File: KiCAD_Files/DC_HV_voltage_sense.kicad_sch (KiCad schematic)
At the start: 17 parts, among them U401 AMC1311BDWVR, U402 MCP6486UT-E/LT

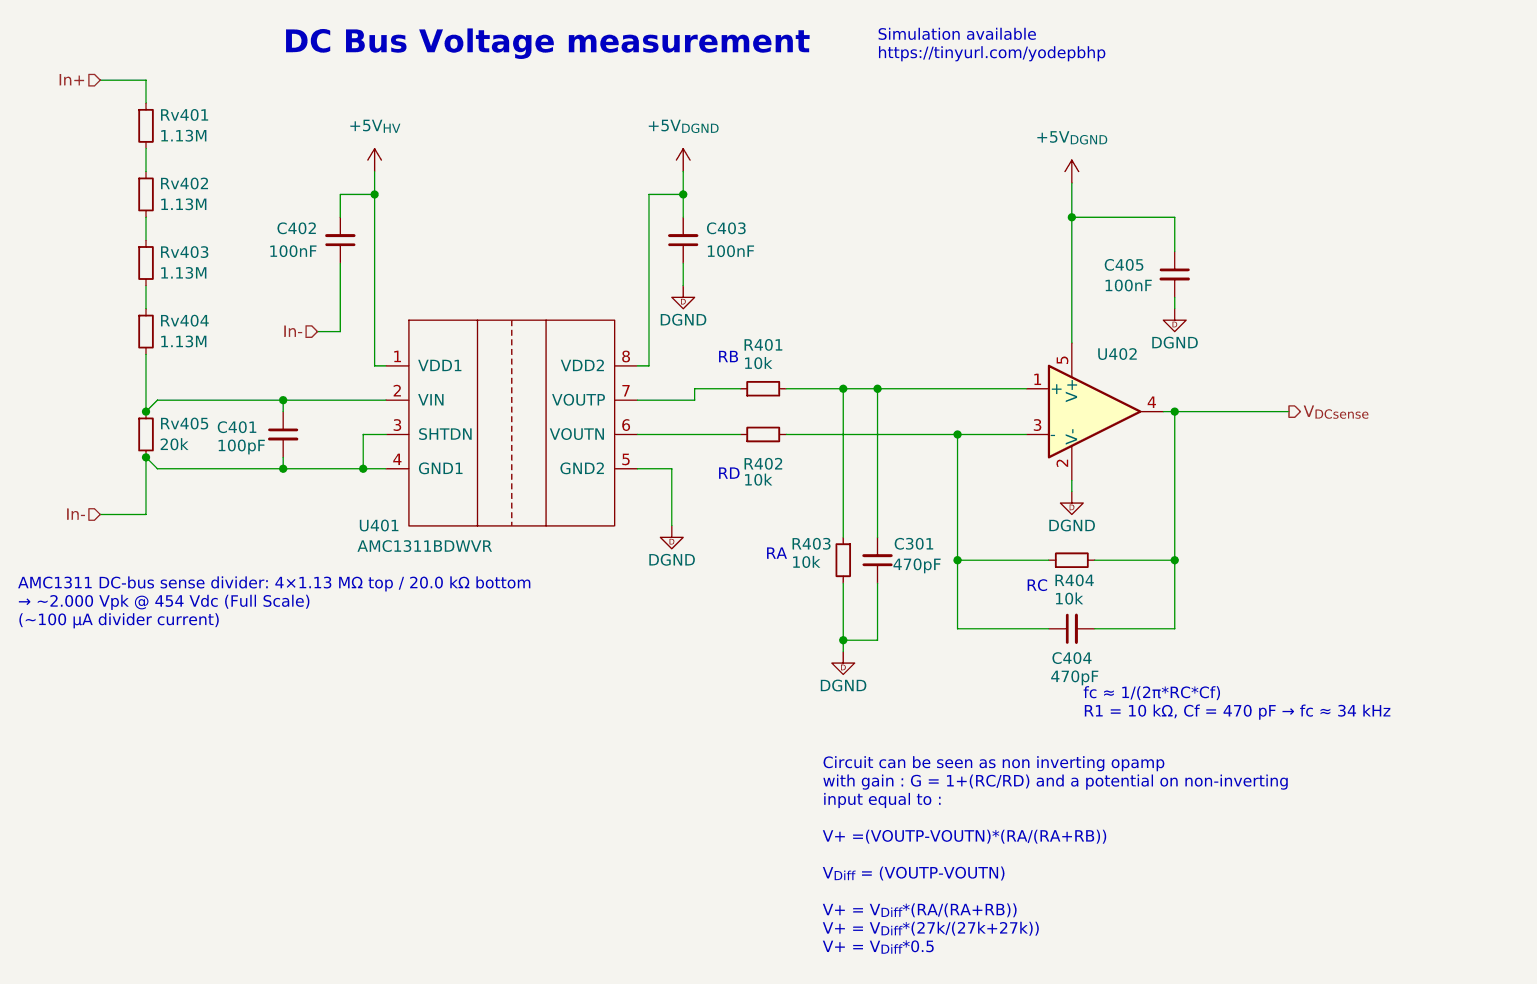
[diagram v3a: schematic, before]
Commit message: Added TL431 for AC measurement 5V regulation. Added more film capacitance. Increased size of 100V ceramic caps to 1210.
Signed-off-by: Jean Alinei <jean.alinei@owntech.org>
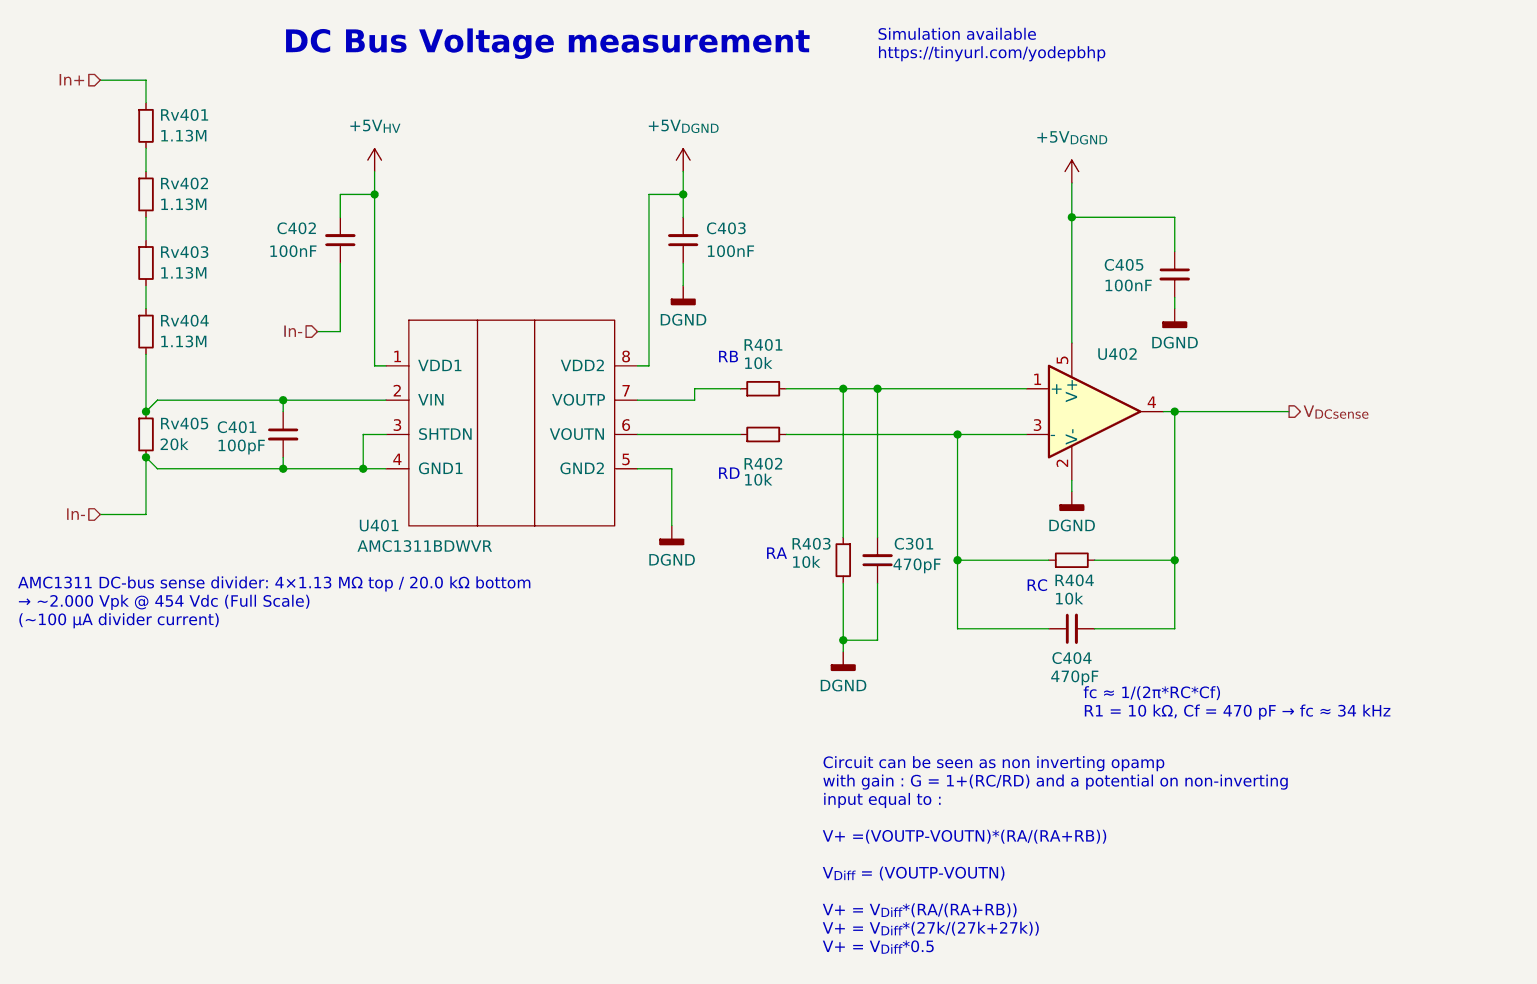
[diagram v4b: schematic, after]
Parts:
- U401: symbol Symbols:AMC1311DBW -> Symbols:AMC1311
- U402: footprint Package_TO_SOT_SMD:SOT-353_SC-70-5_Handsoldering -> Package_TO_SOT_SMD:SOT-353_SC-70-5; symbol Symbols:MCP6486UT-E/LT -> Symbols:MCP6486UT-E/LT
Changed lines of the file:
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@@
 			)
 		)
-		(property "Datasheet" "${KIPRJMOD}\\datasheet\\PYu_RT_1_to_0_01_RoHS_L_12-3003070.pdf"
+		(property "Datasheet" "~"
 			(at 135.89 105.41 0)
 			(effects
@@
 			)
 		)
-		(property "Description" ""
+		(property "Description" "Resistor, small symbol"
 			(at 135.89 105.41 0)
 			(effects
@@
 			)
 		)
-		(property "Description" ""
+		(property "Description" "Resistor, small symbol"
 			(at 33.02 72.39 0)
 			(effects
@@
 	)
 	(symbol
-		(lib_name "R_Small_14")
 		(lib_id "Device:R_Small")
 		(at 101.6 86.36 90)
@@
 			)
 		)
-		(property "Datasheet" "${KIPRJMOD}\\datasheet\\PYu_RT_1_to_0_01_RoHS_L_12-3003070.pdf"
+		(property "Datasheet" "~"
 			(at 101.6 86.36 0)
 			(effects
@@
 			)
 		)
-		(property "Description" ""
+		(property "Description" "Resistor, small symbol"
 			(at 101.6 86.36 0)
 			(effects
@@
 	)
 	(symbol
-		(lib_id "Symbols:DGND")
+		(lib_id "power:GNDD")
 		(at 92.71 74.93 0)
 		(unit 1)
@@
 			)
 		)
-		(property "Description" ""
+		(property "Description" "Power symbol creates a global label with name \"GNDD\" , digital ground"
 			(at 92.71 74.93 0)
 			(effects
@@
 	)
 	(symbol
-		(lib_id "Symbols:+12V_PGND")
+		(lib_id "power:+12V")
 		(at 92.71 62.23 0)
 		(unit 1)
 		(exclude_from_sim no)
-		(in_bom no)
-		(on_board no)
+		(in_bom yes)
+		(on_board yes)
 		(dnp no)
 		(fields_autoplaced yes)
@@
 		)
 		(property "Footprint" ""
-			(at 95.885 59.69 0)
+			(at 92.71 62.23 0)
 			(effects
 				(font
@@
 		)
 		(property "Datasheet" ""
-			(at 95.885 59.69 0)
-			(effects
-				(font
-					(size 1.27 1.27)
-				)
-				(hide yes)
-			)
-		)
-		(property "Description" ""
+			(at 92.71 62.23 0)
+			(effects
+				(font
+					(size 1.27 1.27)
+				)
+				(hide yes)
+			)
+		)
+		(property "Description" "Power symbol creates a global label with name \"+12V\""
 			(at 92.71 62.23 0)
 			(effects
@@
 			)
 		)
-		(property "Datasheet" "${KIPRJMOD}\\datasheet\\PYu_RT_1_to_0_01_RoHS_L_12-3003070.pdf"
+		(property "Datasheet" "~"
 			(at 110.49 105.41 0)
 			(effects
@@
 			)
 		)
-		(property "Description" ""
+		(property "Description" "Resistor, small symbol"
 			(at 110.49 105.41 0)
 			(effects
@@
 	)
 	(symbol
-		(lib_name "R_Small_14")
 		(lib_id "Device:R_Small")
 		(at 101.6 91.44 90)
@@
 			)
 		)
-		(property "Datasheet" "${KIPRJMOD}\\datasheet\\PYu_RT_1_to_0_01_RoHS_L_12-3003070.pdf"
+		(property "Datasheet" "~"
 			(at 101.6 91.44 0)
 			(effects
@@
 			)
 		)
-		(property "Description" ""
+		(property "Description" "Resistor, small symbol"
 			(at 101.6 91.44 0)
 			(effects
@@
 	)
 	(symbol
-		(lib_id "Symbols:DGND")
+		(lib_id "power:GNDD")
 		(at 91.44 101.6 0)
 		(unit 1)
@@
 			)
 		)
-		(property "Description" ""
+		(property "Description" "Power symbol creates a global label with name \"GNDD\" , digital ground"
 			(at 91.44 101.6 0)
 			(effects
@@
 			)
 		)
-		(property "Description" ""
+		(property "Description" "Resistor, small symbol"
 			(at 33.02 80.01 0)
 			(effects
@@
 	)
 	(symbol
-		(lib_id "Symbols:DGND")
+		(lib_id "power:GNDD")
 		(at 135.89 97.79 0)
 		(unit 1)
@@
 			)
 		)
-		(property "Description" ""
+		(property "Description" "Power symbol creates a global label with name \"GNDD\" , digital ground"
 			(at 135.89 97.79 0)
 			(effects
@@
 	)
 	(symbol
-		(lib_id "Symbols:DGND")
+		(lib_id "power:GNDD")
 		(at 147.32 77.47 0)
 		(unit 1)
@@
 			)
 		)
-		(property "Description" ""
+		(property "Description" "Power symbol creates a global label with name \"GNDD\" , digital ground"
 			(at 147.32 77.47 0)
 			(effects
@@
 	)
 	(symbol
-		(lib_name "AMC1311DBW_1")
-		(lib_id "Symbols:AMC1311DBW")
+		(lib_id "Symbols:AMC1311")
 		(at 73.66 91.44 0)
 		(unit 1)
@@
 		)
 		(property "Footprint" "Package_SO:SOIC-8_7.5x5.85mm_P1.27mm"
-			(at 76.2 68.58 0)
-			(effects
-				(font
-					(size 1.27 1.27)
-				)
-				(hide yes)
-			)
-		)
-		(property "Datasheet" "./datasheets/amc1311.pdf"
-			(at 102.87 71.12 0)
-			(effects
-				(font
-					(size 1.27 1.27)
-				)
-				(hide yes)
-			)
-		)
-		(property "Description" ""
+			(at 73.66 97.79 0)
+			(effects
+				(font
+					(size 1.27 1.27)
+				)
+				(hide yes)
+			)
+		)
+		(property "Datasheet" "https://www.ti.com/lit/ds/symlink/amc1311.pdf?ts=1597049043074&ref_url=https%253A%252F%252Fwww.google.com%252F"
+			(at 73.66 97.79 0)
+			(effects
+				(font
+					(size 1.27 1.27)
+				)
+				(hide yes)
+			)
+		)
+		(property "Description" "High-Impedance,2-V Input, Fixed gain:1 - Reinforced Isolated Amplifiers"
 			(at 73.66 91.44 0)
 			(effects
@@
 			)
 		)
-		(property "Description" ""
+		(property "Description" "Resistor, small symbol"
 			(at 33.02 91.44 0)
 			(effects
@@
 	)
 	(symbol
-		(lib_id "Symbols:+12V_PGND")
+		(lib_id "power:+12V")
 		(at 58.42 62.23 0)
 		(unit 1)
 		(exclude_from_sim no)
-		(in_bom no)
-		(on_board no)
+		(in_bom yes)
+		(on_board yes)
 		(dnp no)
 		(fields_autoplaced yes)
@@
 		)
 		(property "Footprint" ""
-			(at 61.595 59.69 0)
+			(at 58.42 62.23 0)
 			(effects
 				(font
@@
 		)
 		(property "Datasheet" ""
-			(at 61.595 59.69 0)
-			(effects
-				(font
-					(size 1.27 1.27)
-				)
-				(hide yes)
-			)
-		)
-		(property "Description" ""
+			(at 58.42 62.23 0)
+			(effects
+				(font
+					(size 1.27 1.27)
+				)
+				(hide yes)
+			)
+		)
+		(property "Description" "Power symbol creates a global label with name \"+12V\""
 			(at 58.42 62.23 0)
 			(effects
@@
 			)
 		)
-		(property "Description" ""
+		(property "Description" "Resistor, small symbol"
 			(at 33.02 64.77 0)
 			(effects
@@
 	)
 	(symbol
-		(lib_id "Symbols:+12V_PGND")
+		(lib_id "power:+12V")
 		(at 135.89 63.5 0)
 		(unit 1)
 		(exclude_from_sim no)
-		(in_bom no)
-		(on_board no)
+		(in_bom yes)
+		(on_board yes)
 		(dnp no)
 		(fields_autoplaced yes)
@@
 		)
 		(property "Footprint" ""
-			(at 139.065 60.96 0)
+			(at 135.89 63.5 0)
 			(effects
 				(font
@@
 		)
 		(property "Datasheet" ""
-			(at 139.065 60.96 0)
-			(effects
-				(font
-					(size 1.27 1.27)
-				)
-				(hide yes)
-			)
-		)
-		(property "Description" ""
 			(at 135.89 63.5 0)
 			(effects
@@
 			)
 		)
+		(property "Description" "Power symbol creates a global label with name \"+12V\""
+			(at 135.89 63.5 0)
+			(effects
+				(font
+					(size 1.27 1.27)
+				)
+				(hide yes)
+			)
+		)
 		(pin "1"
 		)
@@
 	)
 	(symbol
-		(lib_id "Symbols:DGND")
+		(lib_id "power:GNDD")
 		(at 110.49 115.57 0)
 		(unit 1)
@@
 			)
 		)
-		(property "Description" ""
+		(property "Description" "Power symbol creates a global label with name \"GNDD\" , digital ground"
 			(at 110.49 115.57 0)
 			(effects
@@
 	)
 	(symbol
-		(lib_id "Symbols:MCP6486UT-E/LT ")
+		(lib_id "Symbols:MCP6486UT-E/LT")
 		(at 135.89 88.9 0)
 		(unit 1)
@@
 			)
 		)
-		(property "Footprint" "Package_TO_SOT_SMD:SOT-353_SC-70-5_Handsoldering"
+		(property "Footprint" "Package_TO_SOT_SMD:SOT-353_SC-70-5"
 			(at 140.97 95.25 0)
 			(effects
@@
 			)
 		)
-		(property "Description" ""
+		(property "Description" "Resistor, small symbol"
 			(at 33.02 57.15 0)
 			(effects

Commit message: Tidied up the schematic. Added the pdf version for V0.9.
Signed-off-by: Jean Alinei <jean.alinei@owntech.org>
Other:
- title: Micro-inverter - 400W -> DC Bus voltage measurement
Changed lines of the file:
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@@
 	(generator "eeschema")
 	(generator_version "9.0")
-	(paper "A3")
+	(paper "A4")
 	(title_block
-		(title "Micro-inverter - 400W")
-		(date "2024-02-06")
+		(title "DC Bus voltage measurement")
+		(date "2026-01-27")
 		(comment 1 "JAL")
+		(comment 2 "JAL")
+		(comment 3 "JAL")
 	)
 	(text "RB"
@@
 				(width 0)
 				(type dash)
+				(color 0 72 0 1)
 			)
 			(fill
@@
 				(width 0)
 				(type dash)
+				(color 0 0 194 1)
 			)
 			(fill
